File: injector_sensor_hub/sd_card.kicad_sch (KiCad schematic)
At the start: 8 parts, among them J5 Micro_SD_Card

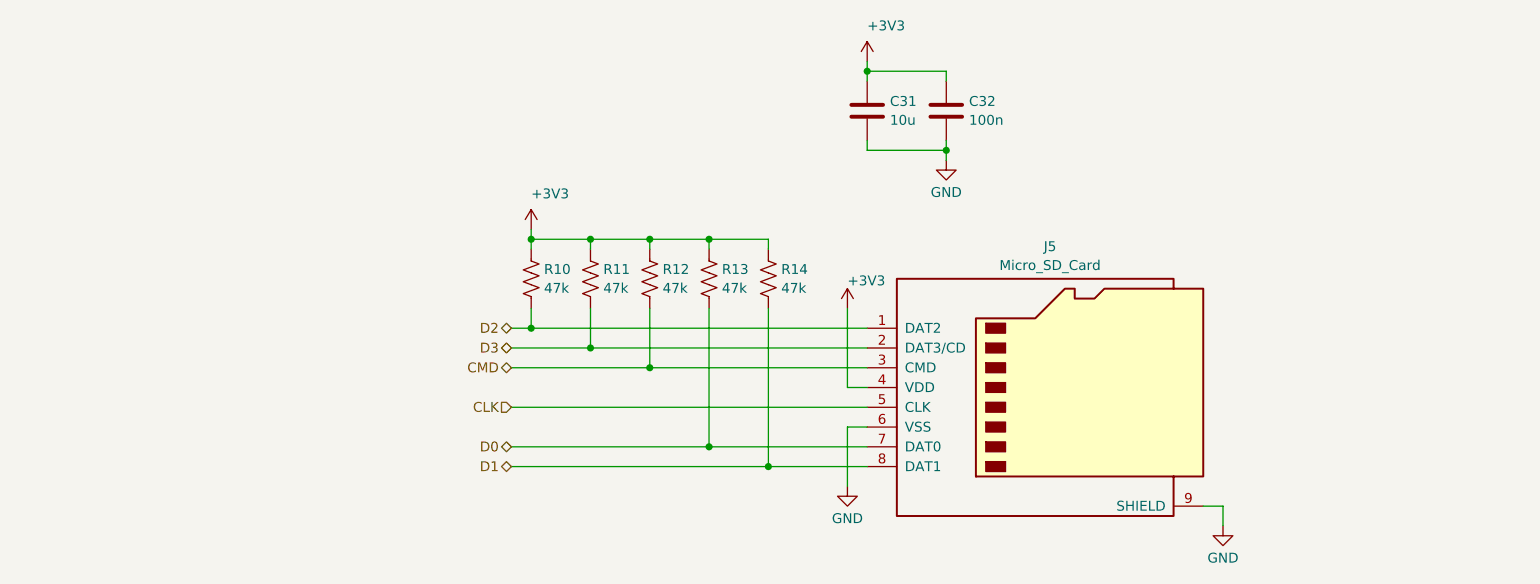
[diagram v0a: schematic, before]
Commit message: Organizing canhw (#145)
Co-authored-by: Jason Huang <91160588+jhuang2006@users.noreply.github.com>
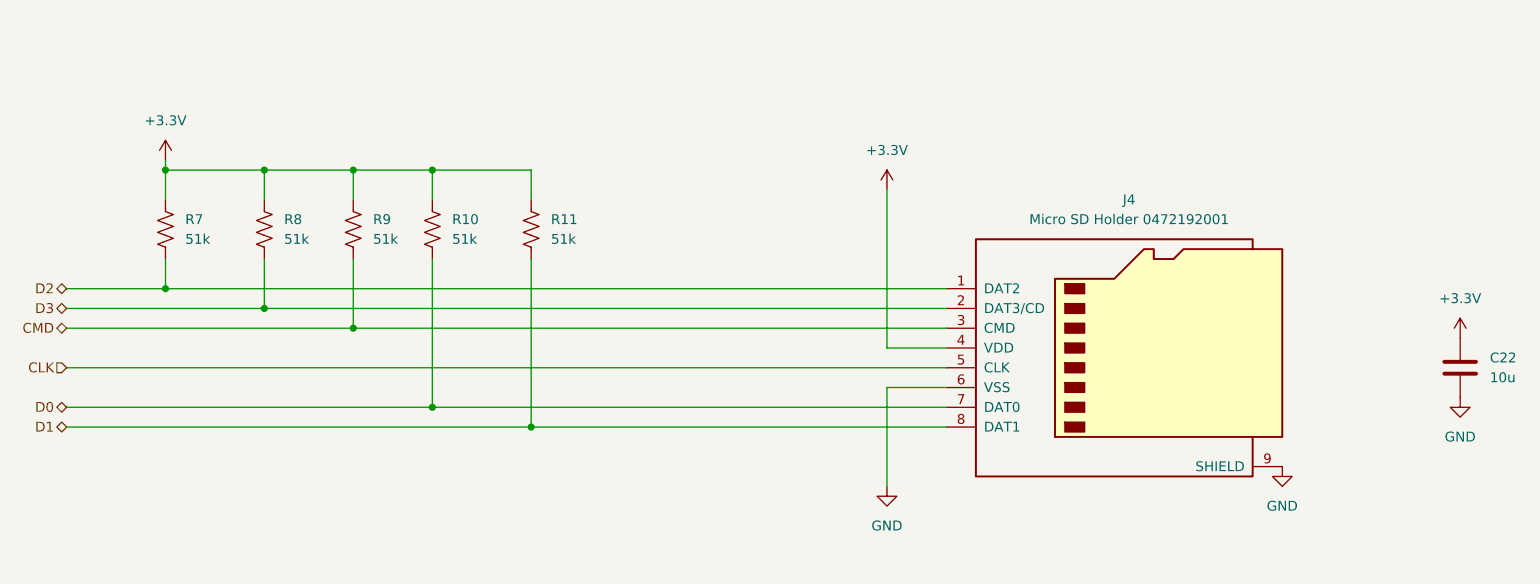
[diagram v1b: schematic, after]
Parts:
- removed C31: 10u, Capacitor_SMD:C_0603_1608Metric_Pad1.08x0.95mm_HandSolder, symbol Device:C
- removed C32: 100n, Capacitor_SMD:C_0603_1608Metric_Pad1.08x0.95mm_HandSolder, symbol Device:C
- removed J5: Micro_SD_Card, canhw_footprints:microSD_Molex_WM6698CT-ND, symbol Connector:Micro_SD_Card
- removed R12, R13, R14: 47k, Resistor_SMD:R_0603_1608Metric_Pad0.98x0.95mm_HandSolder, symbol Device:R_US
- added C22: 10u, Capacitor_SMD:C_0603_1608Metric_Pad1.08x0.95mm_HandSolder, symbol Device:C
- added J4: Micro SD Holder 0472192001, Connector_Card:microSD_HC_Molex_47219-2001, symbol Connector:Micro_SD_Card
- added R7, R8, R9: 51k, Resistor_SMD:R_0603_1608Metric_Pad0.98x0.95mm_HandSolder, symbol Device:R_US
- R10, R11: value 47k -> 51k
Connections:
- net CLK: now also J4.5 (CLK)
- net CMD: now also J4.3 (CMD), R9.2
- net D0: now also R10.2, J4.7 (DAT0)
- net D1: now also R11.2, J4.8 (DAT1)
- net D2: now also J4.1 (DAT2), R7.2; no longer R10.2
- net D3: now also J4.2 (DAT3/CD), R8.2; no longer R11.2
- net GND: now also C22.2, J4.6 (VSS), J4.9 (SHIELD)
- net +3V3 renamed +3.3V
- net +3.3V: now also C22.1, J4.4 (VDD), R7.1, R8.1, R9.1
